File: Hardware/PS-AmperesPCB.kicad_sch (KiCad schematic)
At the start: 12 parts, among them J1 PeripheralCAN, J7 Nanofit 1x05, J8 Nanofit 1x05

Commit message: starting routing i think
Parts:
- J7, J8: footprint (none) -> Connector_Molex:Molex_Nano-Fit_105309-xx05_1x05_P2.50mm_Vertical; P/N 1053131105 -> 1053091105
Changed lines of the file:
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@@
 			)
 		)
-		(property "Footprint" ""
+		(property "Footprint" "Connector_Molex:Molex_Nano-Fit_105309-xx05_1x05_P2.50mm_Vertical"
 			(at 165.1 39.37 0)
 			(effects
@@
 			)
 		)
-		(property "Datasheet" "~"
+		(property "Datasheet" "https://tools.molex.com/pdm_docs/sd/1053091105_sd.pdf"
 			(at 165.1 39.37 0)
 			(effects
@@
 			)
 		)
-		(property "P/N" "1053131105"
+		(property "P/N" "1053091105"
 			(at 165.1 39.37 0)
 			(effects
@@
 			)
 		)
-		(property "Footprint" ""
+		(property "Footprint" "Connector_Molex:Molex_Nano-Fit_105309-xx05_1x05_P2.50mm_Vertical"
 			(at 133.35 39.37 0)
 			(effects
@@
 			)
 		)
-		(property "Datasheet" "~"
+		(property "Datasheet" "https://tools.molex.com/pdm_docs/sd/1053091105_sd.pdf"
 			(at 133.35 39.37 0)
 			(effects
@@
 			)
 		)
-		(property "P/N" "1053131105"
+		(property "P/N" "1053091105"
 			(at 133.35 39.37 0)
 			(effects

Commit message: ye
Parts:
- F2: footprint Fuse:Fuseholder_Blade_Mini_Keystone_3568 -> Parts:FUSE_3568
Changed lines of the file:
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@@
 			)
 		)
-		(property "Footprint" "Fuse:Fuseholder_Blade_Mini_Keystone_3568"
+		(property "Footprint" "Parts:FUSE_3568"
 			(at 166.37 67.818 90)
 			(effects

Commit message: addressed some comments
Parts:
- added R41: 0, Resistor_SMD:R_0603_1608Metric_Pad0.98x0.95mm_HandSolder, symbol Device:R_Small
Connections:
- net +24V_In: now also J7.5 (Pin_5), J8.5 (Pin_5); no longer J7.4 (Pin_4), J8.4 (Pin_4)
- net CAN_HIGH: now also J7.4 (Pin_4), J8.4 (Pin_4); no longer J7.3 (Pin_3), J8.3 (Pin_3)
- net CAN_LOW: now also J7.3 (Pin_3), J8.3 (Pin_3); no longer J7.2 (Pin_2), J8.2 (Pin_2)
- net GND: now also J7.2 (Pin_2), J8.2 (Pin_2), R41.1; no longer J7.1 (Pin_1), J8.1 (Pin_1)
- net ShieldGND: now also J7.1 (Pin_1), J8.1 (Pin_1), R41.2; no longer J7.5 (Pin_5), J8.5 (Pin_5)

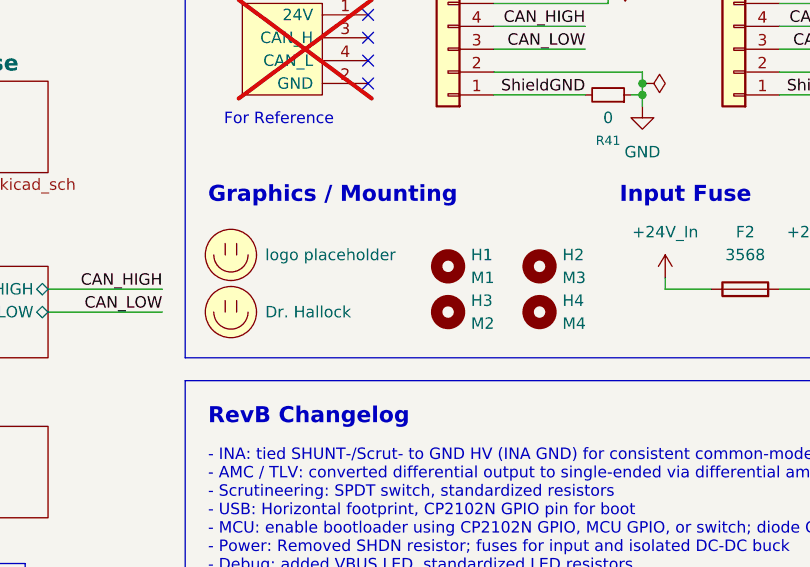
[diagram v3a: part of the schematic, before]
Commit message: added lcsc part numbers
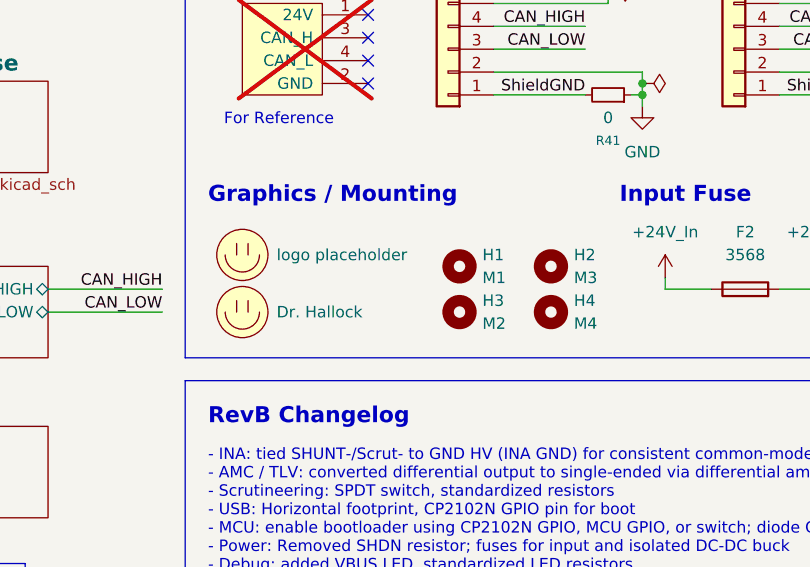
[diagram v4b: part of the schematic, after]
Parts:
- LOGO1, LOGO2, TP19: now left out of the parts list
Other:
- moved on the sheet: H1, H2, H3, H4
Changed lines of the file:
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@@
 	(symbol
 		(lib_id "Mechanical:MountingHole")
-		(at 143.51 63.5 0)
+		(at 144.78 63.5 0)
 		(unit 1)
 		(exclude_from_sim no)
@@
 		(fields_autoplaced yes)
 		(property "Reference" "H2"
-			(at 146.05 62.2299 0)
+			(at 147.32 62.2299 0)
 			(effects
 				(font
@@
 		)
 		(property "Value" "M3"
-			(at 146.05 64.7699 0)
+			(at 147.32 64.7699 0)
 			(effects
 				(font
@@
 		)
 		(property "Footprint" "MountingHole:MountingHole_3.2mm_M3_DIN965_Pad_TopBottom"
-			(at 143.51 63.5 0)
+			(at 144.78 63.5 0)
 			(effects
 				(font
@@
 		)
 		(property "Datasheet" "~"
-			(at 143.51 63.5 0)
+			(at 144.78 63.5 0)
 			(effects
 				(font
@@
 		)
 		(property "Description" "Mounting Hole without connection"
-			(at 143.51 63.5 0)
+			(at 144.78 63.5 0)
 			(effects
 				(font
@@
 		(unit 1)
 		(exclude_from_sim no)
-		(in_bom yes)
+		(in_bom no)
 		(on_board yes)
 		(dnp no)
@@
 	(symbol
 		(lib_id "Mechanical:MountingHole")
-		(at 133.35 68.58 0)
+		(at 134.62 68.58 0)
 		(unit 1)
 		(exclude_from_sim no)
@@
 		(fields_autoplaced yes)
 		(property "Reference" "H3"
-			(at 135.89 67.3099 0)
+			(at 137.16 67.3099 0)
 			(effects
 				(font
@@
 		)
 		(property "Value" "M2"
-			(at 135.89 69.8499 0)
+			(at 137.16 69.8499 0)
 			(effects
 				(font
@@
 		)
 		(property "Footprint" "MountingHole:MountingHole_3.2mm_M3_DIN965_Pad_TopBottom"
-			(at 133.35 68.58 0)
+			(at 134.62 68.58 0)
 			(effects
 				(font
@@
 		)
 		(property "Datasheet" "~"
-			(at 133.35 68.58 0)
+			(at 134.62 68.58 0)
 			(effects
 				(font
@@
 		)
 		(property "Description" "Mounting Hole without connection"
-			(at 133.35 68.58 0)
+			(at 134.62 68.58 0)
 			(effects
 				(font
@@
 		(lib_name "Logo_Placeholder_1")
 		(lib_id "utsvt-misc:Logo_Placeholder")
-		(at 109.22 62.23 0)
-		(unit 1)
-		(exclude_from_sim no)
-		(in_bom yes)
+		(at 110.49 62.23 0)
+		(unit 1)
+		(exclude_from_sim no)
+		(in_bom no)
 		(on_board yes)
 		(dnp no)
 		(fields_autoplaced yes)
 		(property "Reference" "LOGO1"
-			(at 109.22 58.42 0)
+			(at 110.49 58.42 0)
 			(effects
 				(font
@@
 		)
 		(property "Value" "logo placeholder"
-			(at 113.03 62.2299 0)
+			(at 114.3 62.2299 0)
 			(effects
 				(font
@@
 		)
 		(property "Footprint" "UTSVT_Logos:LHRs_LOGO"
-			(at 109.22 60.325 0)
+			(at 110.49 60.325 0)
 			(effects
 				(font
@@
 		)
 		(property "Datasheet" ""
-			(at 109.22 60.325 0)
+			(at 110.49 60.325 0)
 			(effects
 				(font
@@
 		)
 		(property "Description" "Graph footprint placeholder"
-			(at 109.22 62.23 0)
+			(at 110.49 62.23 0)
 			(effects
 				(font
@@
 		)
 		(property "PN" ""
-			(at 109.22 62.23 0)
+			(at 110.49 62.23 0)
 			(effects
 				(font
@@
 		)
 		(property "p/n" ""
-			(at 109.22 62.23 0)
+			(at 110.49 62.23 0)
 			(effects
 				(font
@@
 	(symbol
 		(lib_id "Mechanical:MountingHole")
-		(at 143.51 68.58 0)
+		(at 144.78 68.58 0)
 		(unit 1)
 		(exclude_from_sim no)
@@
 		(fields_autoplaced yes)
 		(property "Reference" "H4"
-			(at 146.05 67.3099 0)
+			(at 147.32 67.3099 0)
 			(effects
 				(font
@@
 		)
 		(property "Value" "M4"
-			(at 146.05 69.8499 0)
+			(at 147.32 69.8499 0)
 			(effects
 				(font
@@
 		)
 		(property "Footprint" "MountingHole:MountingHole_3.2mm_M3_DIN965_Pad_TopBottom"
-			(at 143.51 68.58 0)
+			(at 144.78 68.58 0)
 			(effects
 				(font
@@
 		)
 		(property "Datasheet" "~"
-			(at 143.51 68.58 0)
+			(at 144.78 68.58 0)
 			(effects
 				(font
@@
 		)
 		(property "Description" "Mounting Hole without connection"
-			(at 143.51 68.58 0)
+			(at 144.78 68.58 0)
 			(effects
 				(font
@@
 	(symbol
 		(lib_id "utsvt-misc:Logo_Placeholder")
-		(at 109.22 68.58 0)
-		(unit 1)
-		(exclude_from_sim no)
-		(in_bom yes)
+		(at 110.49 68.58 0)
+		(unit 1)
+		(exclude_from_sim no)
+		(in_bom no)
 		(on_board yes)
 		(dnp no)
 		(fields_autoplaced yes)
 		(property "Reference" "LOGO2"
-			(at 109.22 64.77 0)
+			(at 110.49 64.77 0)
 			(effects
 				(font
@@
 		)
 		(property "Value" "Dr. Hallock"
-			(at 113.03 68.5799 0)
+			(at 114.3 68.5799 0)
 			(effects
 				(font
@@
 		)
 		(property "Footprint" "UTSVT_Logos:Hallock_Image_Tiny"
-			(at 109.22 66.675 0)
+			(at 110.49 66.675 0)
 			(effects
 				(font
@@
 		)
 		(property "Datasheet" ""
-			(at 109.22 66.675 0)
+			(at 110.49 66.675 0)
 			(effects
 				(font
@@
 		)
 		(property "Description" "Graph footprint placeholder"
-			(at 109.22 68.58 0)
+			(at 110.49 68.58 0)
 			(effects
 				(font
@@
 		)
 		(property "PN" ""
-			(at 109.22 68.58 0)
+			(at 110.49 68.58 0)
 			(effects
 				(font
@@
 		)
 		(property "p/n" ""
-			(at 109.22 68.58 0)
+			(at 110.49 68.58 0)
 			(effects
 				(font
@@
 	(symbol
 		(lib_id "Mechanical:MountingHole")
-		(at 133.35 63.5 0)
+		(at 134.62 63.5 0)
 		(unit 1)
 		(exclude_from_sim no)
@@
 		(fields_autoplaced yes)
 		(property "Reference" "H1"
-			(at 135.89 62.2299 0)
+			(at 137.16 62.2299 0)
 			(effects
 				(font
@@
 		)
 		(property "Value" "M1"
-			(at 135.89 64.7699 0)
+			(at 137.16 64.7699 0)
 			(effects
 				(font
@@
 		)
 		(property "Footprint" "MountingHole:MountingHole_3.2mm_M3_DIN965_Pad_TopBottom"
-			(at 133.35 63.5 0)
+			(at 134.62 63.5 0)
 			(effects
 				(font
@@
 		)
 		(property "Datasheet" "~"
-			(at 133.35 63.5 0)
+			(at 134.62 63.5 0)
 			(effects
 				(font
@@
 		)
 		(property "Description" "Mounting Hole without connection"
-			(at 133.35 63.5 0)
-			(effects
-				(font
+			(at 134.62 63.5 0)
+			(effects
+				(font
